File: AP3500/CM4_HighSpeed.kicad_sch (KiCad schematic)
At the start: 1 part

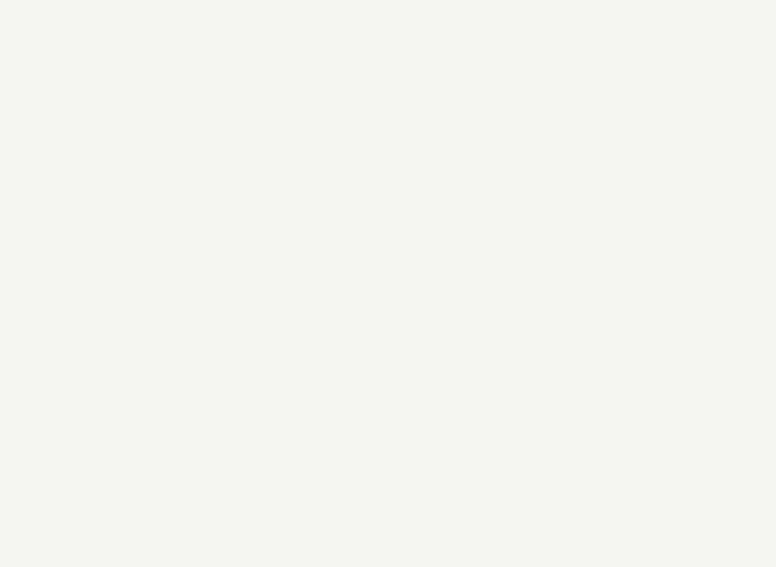
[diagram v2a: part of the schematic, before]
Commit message: Add new single polarity aperture coupled 4x4 antenna. RasPiCNM4Connector test Gerbers for PCBWay Cleanups and optimixations for AP3500
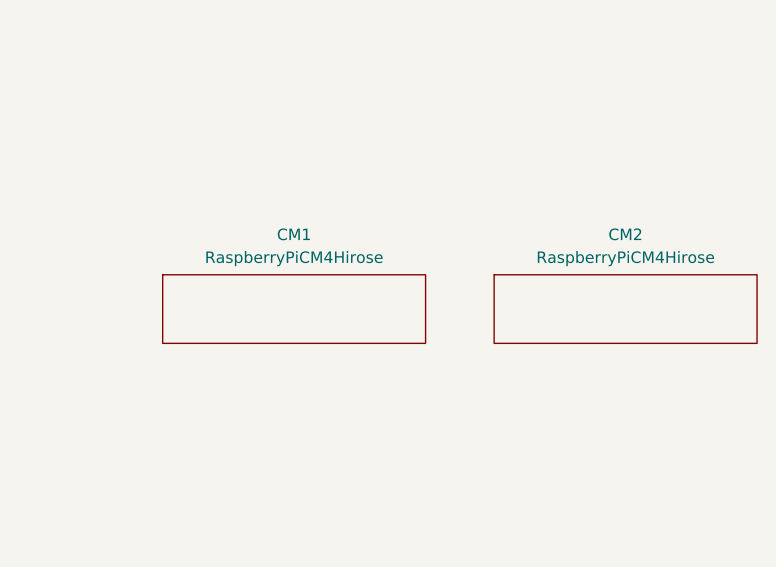
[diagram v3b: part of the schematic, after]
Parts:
- added CM1, CM2: RaspberryPiCM4Hirose, AP3000:Hirose-DF40C-100DS-0.4V, symbol AP3000:RaspberryPiCM4Hirose
- Module1: footprint AP3500:Raspberry-Pi-4-Compute-Module -> AP3000:Raspberry-Pi-4-Compute-Module; now left out of the parts list
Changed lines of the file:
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@@
-(kicad_sch (version 20210126) (generator eeschema)
+(kicad_sch (version 20210406) (generator eeschema)
   (paper "A4")
   (title_block
@@
     (pin "1")
   )
+  (symbol (lib_id "AP3000:RaspberryPiCM4Hirose") (at 148.59 80.645 0) (unit 1)
+    (in_bom yes) (on_board yes) (fields_autoplaced)
+    (property "Reference" "CM1" (id 0) (at 151.765 72.39 0))
+    (property "Value" "RaspberryPiCM4Hirose" (id 1) (at 151.765 74.93 0))
+    (property "Footprint" "AP3000:Hirose-DF40C-100DS-0.4V" (id 2) (at 148.59 80.645 0)
+      (effects (font (size 1.27 1.27)) hide)
+    )
+    (property "Datasheet" "" (id 3) (at 148.59 80.645 0)
+      (effects (font (size 1.27 1.27)) hide)
+    )
+    (property "LCSC" "C424649" (id 4) (at 148.59 80.645 0)
+      (effects (font (size 1.27 1.27)) hide)
+    )
+  )
+  (symbol (lib_id "AP3000:RaspberryPiCM4Hirose") (at 185.42 80.645 0) (unit 1)
+    (in_bom yes) (on_board yes) (fields_autoplaced)
+    (property "Reference" "CM2" (id 0) (at 188.595 72.39 0))
+    (property "Value" "RaspberryPiCM4Hirose" (id 1) (at 188.595 74.93 0))
+    (property "Footprint" "AP3000:Hirose-DF40C-100DS-0.4V" (id 2) (at 185.42 80.645 0)
+      (effects (font (size 1.27 1.27)) hide)
+    )
+    (property "Datasheet" "" (id 3) (at 185.42 80.645 0)
+      (effects (font (size 1.27 1.27)) hide)
+    )
+    (property "LCSC" "C424649" (id 4) (at 185.42 80.645 0)
+      (effects (font (size 1.27 1.27)) hide)
+    )
+  )
   (symbol (lib_id "AP3500:ComputeModule4-CM4") (at -67.31 87.63 0) (unit 2)
-    (in_bom yes) (on_board yes)
+    (in_bom no) (on_board yes)
     (property "Reference" "Module1" (id 0) (at 72.39 15.367 0))
     (property "Value" "ComputeModule4" (id 1) (at 72.39 17.6784 0))
-    (property "Footprint" "AP3500:Raspberry-Pi-4-Compute-Module" (id 2) (at 74.93 114.3 0)
+    (property "Footprint" "AP3000:Raspberry-Pi-4-Compute-Module" (id 2) (at 74.93 114.3 0)
       (effects (font (size 1.27 1.27)) hide)
     )
@@
       (effects (font (size 1.27 1.27)) hide)
     )
-    (property "PartsBoxID" "DF40C-100DS-0.4V(51)" (id 4) (at -67.31 87.63 0)
-      (effects (font (size 1.27 1.27)) hide)
-    )
+    (property "PartsBoxID" "DF40C-100DS-0.4V(51)" (id 9) (at -67.31 87.63 0)
+      (effects (font (size 1.27 1.27)) hide)
+    )
